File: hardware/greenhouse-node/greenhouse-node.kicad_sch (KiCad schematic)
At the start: 25 parts

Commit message: First PCB design for node
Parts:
- removed C?: 100uF, symbol Device:C_Polarized_Small
- removed D?: 1N4001, Diode_THT:D_DO-41_SOD81_P10.16mm_Horizontal, symbol Diode:1N4001
- removed J?: Conn_01x02_Male, symbol Connector:Conn_01x02_Male
- C2: renamed from C?; value 100nF -> 330nF
- D1, D2, D3, D4: renamed from D?; footprint (none) -> LED_THT:LED_D3.0mm
- J1: renamed from J?; footprint (none) -> Connector_Molex:Molex_KK-254_AE-6410-12A_1x12_P2.54mm_Vertical
- J2: renamed from J?; footprint (none) -> Connector_Molex:Molex_KK-254_AE-6410-02A_1x02_P2.54mm_Vertical
- J3: renamed from J?; footprint (none) -> Connector_Molex:Molex_KK-396_A-41791-0002_1x02_P3.96mm_Vertical
- J5: renamed from J?; footprint Connector_Molex:Molex_KK-254_AE-6410-08A_1x04_P2.54mm_Vertical -> Connector_PinHeader_2.54mm:PinHeader_1x04_P2.54mm_Vertical
- R1, R2, R3, R4: renamed from R?; footprint (none) -> Resistor_THT:R_Axial_DIN0204_L3.6mm_D1.6mm_P7.62mm_Horizontal
- SW1: renamed from SW?; footprint (none) -> Button_Switch_THT:SW_PUSH_6mm
- U2: renamed from U?; footprint (none) -> Package_TO_SOT_THT:TO-220-3_Horizontal_TabDown
- U3: renamed from U?; footprint (none) -> Package_DIP:DIP-16_W7.62mm_Socket
- gave numbers to parts that had none: 6
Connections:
- net +12V: now also C2.2, U2.1 (IN)

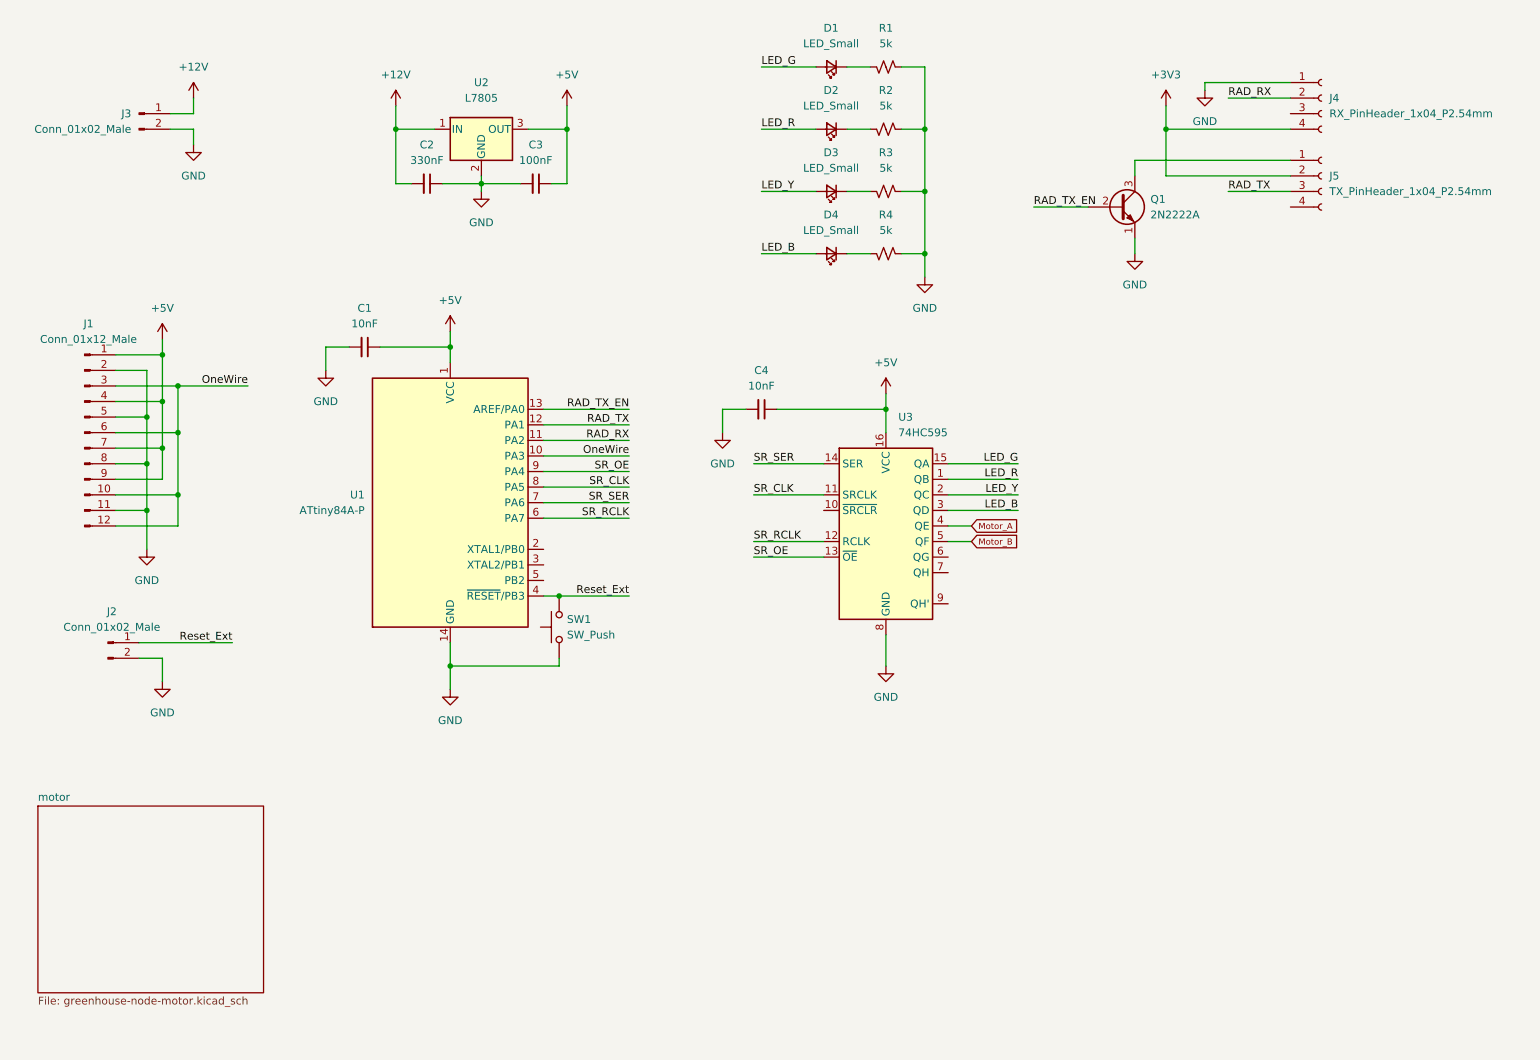
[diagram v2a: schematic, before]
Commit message: Redesign node PCB around mounting holes
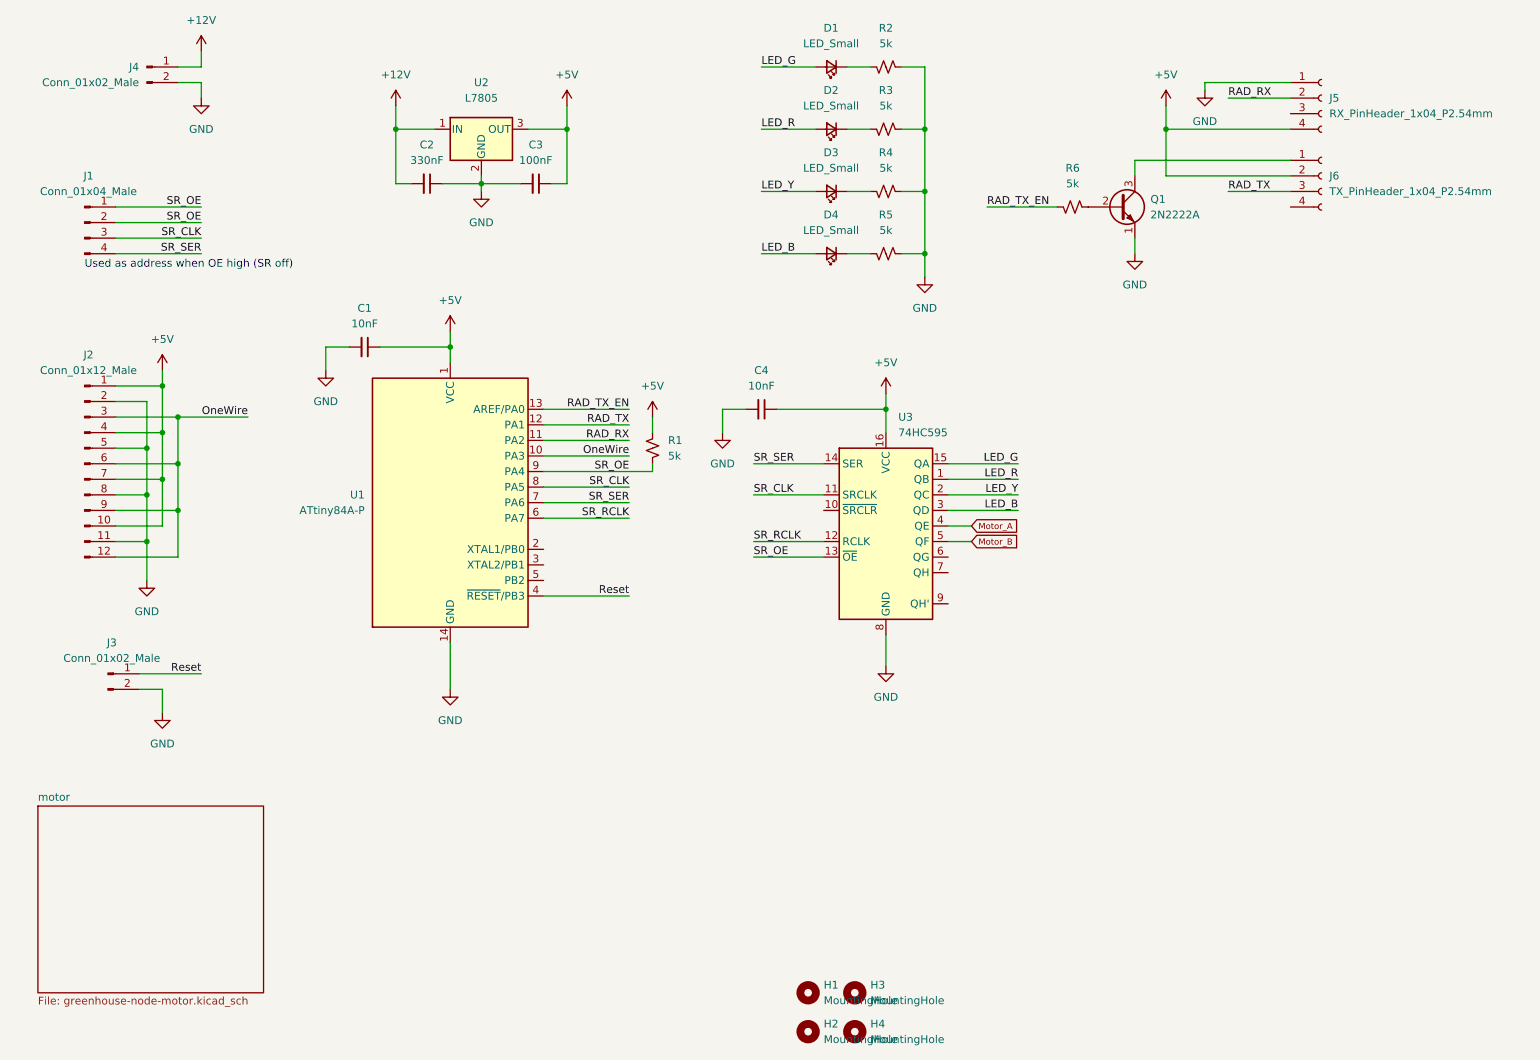
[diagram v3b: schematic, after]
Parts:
- removed SW1: SW_Push, Button_Switch_THT:SW_PUSH_6mm, symbol Switch:SW_Push
- added H1, H2, H3, H4: MountingHole, MountingHole:MountingHole_3.2mm_M3, symbol Mechanical:MountingHole
- added J1: Conn_01x04_Male, Connector_PinHeader_2.54mm:PinHeader_2x02_P2.54mm_Vertical, symbol Connector:Conn_01x04_Male
- added R1, R6: 5k, Resistor_THT:R_Axial_DIN0204_L3.6mm_D1.6mm_P7.62mm_Horizontal, symbol Device:R_Small_US
- J5: renamed from J4; footprint Connector_PinHeader_2.54mm:PinHeader_1x04_P2.54mm_Vertical -> Connector_PinSocket_2.54mm:PinSocket_1x04_P2.54mm_Vertical
- J6: renamed from J5; footprint Connector_PinHeader_2.54mm:PinHeader_1x04_P2.54mm_Vertical -> Connector_PinSocket_2.54mm:PinSocket_1x04_P2.54mm_Vertical
- U1: footprint Package_DIP:DIP-14_W7.62mm -> Package_DIP:DIP-14_W7.62mm_Socket
- renumbered J1 to J2, J2 to J3, J3 to J4, R1 to R2, R2 to R3, R3 to R4, R4 to R5
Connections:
- net +3V3 is gone; now on net +5V: J5.4 (Pin_4), J6.2 (Pin_2)
- net +5V: now also J2.10 (Pin_10), R1.1; no longer J2.9 (Pin_9)
- net OneWire: now also J2.9 (Pin_9); no longer J2.10 (Pin_10)
- net RAD_TX_EN: now also R6.2; no longer Q1.2 (B)
- net SR_CLK: now also J1.3 (Pin_3)
- net SR_OE: now also J1.1 (Pin_1), J1.2 (Pin_2), R1.2
- net SR_SER: now also J1.4 (Pin_4)
- net Reset_Ext renamed Reset
- new net: Q1.2 (B), R6.1
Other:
- note added: "Used as address when OE high (SR off)"
- moved on the sheet: J2, J3, J4

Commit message: Fixed missing traces
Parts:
- Q1: value 2N2222A -> BC549C; symbol Nick:2N2222A -> Transistor_BJT:BC549
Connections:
- net GND: now also Q1.3 (E); no longer Q1.1 (E)
- net at J6.1 (Pin_1): now also Q1.1 (C); no longer Q1.3 (C)
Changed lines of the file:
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@@
     (pin "9")
   )
-  (symbol (lib_id "Nick:2N2222A") (at 210.82 55.88 0) (unit 1)
+  (symbol (lib_id "Transistor_BJT:BC549") (at 210.82 55.88 0) (unit 1)
     (in_bom yes) (on_board yes) (fields_autoplaced)
     (property "Reference" "Q1" (id 0) (at 215.9 54.6099 0)
       (effects (font (size 1.27 1.27)) (justify left))
     )
-    (property "Value" "2N2222A" (id 1) (at 215.9 57.1499 0)
+    (property "Value" "BC549C" (id 1) (at 215.9 57.1499 0)
       (effects (font (size 1.27 1.27)) (justify left))
     )
@@
       (effects (font (size 1.27 1.27) italic) (justify left) hide)
     )
-    (property "Datasheet" "https://www.onsemi.com/pub/Collateral/2N3903-D.PDF" (id 3) (at 210.82 55.88 0)
+    (property "Datasheet" "https://www.onsemi.com/pub/Collateral/BC550-D.pdf" (id 3) (at 210.82 55.88 0)
       (effects (font (size 1.27 1.27)) (justify left) hide)
     )
@@
       (reference "#PWR019") (unit 1) (value "GND") (footprint "")
     )
+    (path "/f125db1d-864d-4c2f-aa44-ac14276ec569/42979d9c-45c7-44ea-b09e-664b9987e3cb"
+      (reference "#PWR020") (unit 1) (value "+12V") (footprint "")
+    )
     (path "/f125db1d-864d-4c2f-aa44-ac14276ec569/eb83045a-3265-4cb3-a640-fc71123b572b"
-      (reference "#PWR020") (unit 1) (value "GND") (footprint "")
-    )
-    (path "/f125db1d-864d-4c2f-aa44-ac14276ec569/42979d9c-45c7-44ea-b09e-664b9987e3cb"
-      (reference "#PWR021") (unit 1) (value "+12V") (footprint "")
+      (reference "#PWR021") (unit 1) (value "GND") (footprint "")
     )
     (path "/f125db1d-864d-4c2f-aa44-ac14276ec569/4094f064-5398-4528-94a6-9af7303eefd2"
-      (reference "#PWR023") (unit 1) (value "GND") (footprint "")
+      (reference "#PWR022") (unit 1) (value "GND") (footprint "")
     )
     (path "/f125db1d-864d-4c2f-aa44-ac14276ec569/4555a28c-f6f1-4471-86dd-c79e1eb5f92d"
-      (reference "#PWR024") (unit 1) (value "+10V") (footprint "")
+      (reference "#PWR023") (unit 1) (value "+10V") (footprint "")
     )
     (path "/f125db1d-864d-4c2f-aa44-ac14276ec569/e88ece75-9a94-418e-ae4c-0a8217f9cfbb"
+      (reference "#PWR024") (unit 1) (value "GND") (footprint "")
+    )
+    (path "/f125db1d-864d-4c2f-aa44-ac14276ec569/e3c32dad-56ae-40c1-b262-607020b74545"
       (reference "#PWR025") (unit 1) (value "GND") (footprint "")
     )
-    (path "/f125db1d-864d-4c2f-aa44-ac14276ec569/e3c32dad-56ae-40c1-b262-607020b74545"
-      (reference "#PWR026") (unit 1) (value "GND") (footprint "")
-    )
     (path "/f125db1d-864d-4c2f-aa44-ac14276ec569/0b9c82ff-229c-4ba3-86ae-ce5fc883bef6"
-      (reference "#PWR027") (unit 1) (value "+12V") (footprint "")
+      (reference "#PWR026") (unit 1) (value "+12V") (footprint "")
+    )
+    (path "/f125db1d-864d-4c2f-aa44-ac14276ec569/faa75408-7bc9-47b9-8a84-b71947d6e554"
+      (reference "#PWR027") (unit 1) (value "GND") (footprint "")
     )
     (path "/f125db1d-864d-4c2f-aa44-ac14276ec569/7edb6214-ff1b-45cd-bece-105eb508f1e9"
-      (reference "#PWR029") (unit 1) (value "+10V") (footprint "")
+      (reference "#PWR028") (unit 1) (value "+10V") (footprint "")
     )
     (path "/f125db1d-864d-4c2f-aa44-ac14276ec569/24032f1c-92ba-4478-9c3a-62b699462be2"
-      (reference "#PWR031") (unit 1) (value "GND") (footprint "")
-    )
-    (path "/f125db1d-864d-4c2f-aa44-ac14276ec569/faa75408-7bc9-47b9-8a84-b71947d6e554"
-      (reference "#PWR?") (unit 1) (value "GND") (footprint "")
+      (reference "#PWR029") (unit 1) (value "GND") (footprint "")
     )
     (path "/1bbe0bee-1018-4ce9-bd17-02581403417d"
@@
     )
     (path "/9d5e7df5-7472-4dc8-a9fc-73987a422b16"
-      (reference "Q1") (unit 1) (value "2N2222A") (footprint "Package_TO_SOT_THT:TO-92_Inline")
+      (reference "Q1") (unit 1) (value "BC549C") (footprint "Package_TO_SOT_THT:TO-92_Inline")
     )
     (path "/f125db1d-864d-4c2f-aa44-ac14276ec569/6f8b4a11-5387-48d0-886f-b5d7c4164d33"
-      (reference "Q2") (unit 1) (value "2N2222A") (footprint "Package_TO_SOT_THT:TO-92_Inline")
+      (reference "Q2") (unit 1) (value "BC549C") (footprint "Package_TO_SOT_THT:TO-92_Inline")
     )
     (path "/f125db1d-864d-4c2f-aa44-ac14276ec569/33e96e22-a856-4e33-be56-a2067ce30139"
-      (reference "Q4") (unit 1) (value "IRF9530N") (footprint "Package_TO_SOT_THT:TO-220-3_Horizontal_TabDown")
+      (reference "Q3") (unit 1) (value "IRF9530N") (footprint "Package_TO_SOT_THT:TO-220-3_Horizontal_TabDown")
     )
     (path "/f125db1d-864d-4c2f-aa44-ac14276ec569/7d9a76cb-fc0e-40b0-a0c3-02f1f235f41f"
-      (reference "Q5") (unit 1) (value "IRF530N") (footprint "Package_TO_SOT_THT:TO-220-3_Horizontal_TabDown")
+      (reference "Q4") (unit 1) (value "IRF530N") (footprint "Package_TO_SOT_THT:TO-220-3_Horizontal_TabDown")
     )
     (path "/f125db1d-864d-4c2f-aa44-ac14276ec569/4776eb62-0319-43f7-a210-29442a9c84c1"
-      (reference "Q6") (unit 1) (value "FDP7030DL") (footprint "Package_TO_SOT_THT:TO-220-3_Horizontal_TabDown")
+      (reference "Q5") (unit 1) (value "FDP7030DL") (footprint "Package_TO_SOT_THT:TO-220-3_Horizontal_TabDown")
     )
     (path "/f125db1d-864d-4c2f-aa44-ac14276ec569/6ea00187-9c84-4f7e-91e0-78d37efe1b8e"
-      (reference "Q7") (unit 1) (value "IRF9530N") (footprint "Package_TO_SOT_THT:TO-220-3_Horizontal_TabDown")
+      (reference "Q6") (unit 1) (value "IRF9530N") (footprint "Package_TO_SOT_THT:TO-220-3_Horizontal_TabDown")
     )
     (path "/f125db1d-864d-4c2f-aa44-ac14276ec569/e32ac39b-5561-422e-859f-0e71182c501b"
-      (reference "Q8") (unit 1) (value "IRF530N") (footprint "Package_TO_SOT_THT:TO-220-3_Horizontal_TabDown")
+      (reference "Q7") (unit 1) (value "IRF530N") (footprint "Package_TO_SOT_THT:TO-220-3_Horizontal_TabDown")
     )
     (path "/f125db1d-864d-4c2f-aa44-ac14276ec569/1911228a-67c7-4d68-a713-05769cb11287"
-      (reference "Q?") (unit 1) (value "2N2222A") (footprint "Package_TO_SOT_THT:TO-92_Inline")
+      (reference "Q8") (unit 1) (value "BC549C") (footprint "Package_TO_SOT_THT:TO-92_Inline")
     )
     (path "/302b2aa9-738c-4aa7-b455-5a902820fe10"
@@
       (reference "R7") (unit 1) (value "1k") (footprint "Resistor_THT:R_Axial_DIN0204_L3.6mm_D1.6mm_P7.62mm_Horizontal")
     )
+    (path "/f125db1d-864d-4c2f-aa44-ac14276ec569/b9d2c99b-3cf7-4aa0-9bcc-46f3a3c90e29"
+      (reference "R8") (unit 1) (value "10k") (footprint "Resistor_THT:R_Axial_DIN0204_L3.6mm_D1.6mm_P7.62mm_Horizontal")
+    )
     (path "/f125db1d-864d-4c2f-aa44-ac14276ec569/d33d0fb3-6d1f-4cc7-b00d-5d21fba58dee"
+      (reference "R9") (unit 1) (value "10k") (footprint "Resistor_THT:R_Axial_DIN0204_L3.6mm_D1.6mm_P7.62mm_Horizontal")
+    )
+    (path "/f125db1d-864d-4c2f-aa44-ac14276ec569/bf817e6d-58a1-41ad-a248-45e7818135e2"
       (reference "R10") (unit 1) (value "10k") (footprint "Resistor_THT:R_Axial_DIN0204_L3.6mm_D1.6mm_P7.62mm_Horizontal")
     )
+    (path "/f125db1d-864d-4c2f-aa44-ac14276ec569/9ae45e59-c118-40ec-a648-86011e953bd8"
+      (reference "R11") (unit 1) (value "1k") (footprint "Resistor_THT:R_Axial_DIN0204_L3.6mm_D1.6mm_P7.62mm_Horizontal")
+    )
     (path "/f125db1d-864d-4c2f-aa44-ac14276ec569/df623628-765e-4325-b9a9-cd3733e8b26f"
-      (reference "R14") (unit 1) (value "5k") (footprint "Resistor_THT:R_Axial_DIN0204_L3.6mm_D1.6mm_P7.62mm_Horizontal")
+      (reference "R12") (unit 1) (value "5k") (footprint "Resistor_THT:R_Axial_DIN0204_L3.6mm_D1.6mm_P7.62mm_Horizontal")
     )
     (path "/f125db1d-864d-4c2f-aa44-ac14276ec569/df565b59-55c6-4aa6-b4bc-30a03a18a15b"
-      (reference "R15") (unit 1) (value "5k") (footprint "Resistor_THT:R_Axial_DIN0204_L3.6mm_D1.6mm_P7.62mm_Horizontal")
-    )
-    (path "/f125db1d-864d-4c2f-aa44-ac14276ec569/9ae45e59-c118-40ec-a648-86011e953bd8"
-      (reference "R?") (unit 1) (value "1k") (footprint "Resistor_THT:R_Axial_DIN0204_L3.6mm_D1.6mm_P7.62mm_Horizontal")
-    )
-    (path "/f125db1d-864d-4c2f-aa44-ac14276ec569/b9d2c99b-3cf7-4aa0-9bcc-46f3a3c90e29"
-      (reference "R?") (unit 1) (value "10k") (footprint "Resistor_THT:R_Axial_DIN0204_L3.6mm_D1.6mm_P7.62mm_Horizontal")
-    )
-    (path "/f125db1d-864d-4c2f-aa44-ac14276ec569/bf817e6d-58a1-41ad-a248-45e7818135e2"
-      (reference "R?") (unit 1) (value "10k") (footprint "Resistor_THT:R_Axial_DIN0204_L3.6mm_D1.6mm_P7.62mm_Horizontal")
+      (reference "R13") (unit 1) (value "5k") (footprint "Resistor_THT:R_Axial_DIN0204_L3.6mm_D1.6mm_P7.62mm_Horizontal")
     )
     (path "/9753ff07-d111-4956-af59-0c4add831580"
